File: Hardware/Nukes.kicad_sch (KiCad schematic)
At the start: 25 parts, among them J6 Screw_Terminal_01x08, J7 Conn_01x05_Male, Q2 NCV8415STT1G, Q3 NCV8415STT1G, Q4 NCV8415STT1G, Q5 NCV8415STT1G, U3 LTV-247, U4 PCA9534RGVR, U5 PCA9685BS

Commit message: v3 hardware start
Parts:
- removed Q2, Q3, Q4, Q5: NCV8415STT1G, Package_TO_SOT_SMD:SOT-223, symbol Driver_FET:NCV8402xST
- added Q2, Q3, Q4, Q5: BUK9M11-40EX, Package_TO_SOT_SMD:LFPAK33, symbol Transistor_FET:BUK9M11-40EX
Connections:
- net SERVO4 is gone; now on net SERVO3: J7.5 (Pin_5), U5.14 (LED10)
- net Cont1: now also R18.1, U3.13, U4.4 (P2); no longer R22.1, U3.9, U4.9 (P6)
- net Cont3: now also R22.1, U3.9, U4.9 (P6); no longer R18.1, U3.13, U4.4 (P2)
- net GND: now also Q2.1 (S), Q2.2 (S), Q2.3 (S), Q3.1 (S), Q3.2 (S), Q3.3 (S), Q4.1 (S), Q4.2 (S), Q4.3 (S), Q5.1 (S), Q5.2 (S), Q5.3 (S)
- net Nuke1: now also U4.5 (P3), Q2.4 (G); no longer U4.10 (P7)
- net Nuke1-: now also D8.1 (A), D8.2 (A), J6.3 (Pin_3), U3.3; no longer D10.1 (A), D10.2 (A), J6.7 (Pin_7), U3.7
- net Nuke2: now also Q5.4 (G)
- net Nuke3: now also U4.10 (P7), Q4.4 (G); no longer U4.5 (P3)
- net Nuke3-: now also D10.1 (A), D10.2 (A), J6.7 (Pin_7), U3.7; no longer D8.1 (A), D8.2 (A), J6.3 (Pin_3), U3.3
- net SERVO1: now also J7.3 (Pin_3), U5.12 (LED8); no longer J7.2 (Pin_2), U5.10 (LED7)
- net SERVO2: now also J7.4 (Pin_4), U5.13 (LED9); no longer J7.3 (Pin_3), U5.12 (LED8)
- net SERVO3: no longer J7.4 (Pin_4), U5.13 (LED9)
- net at D10.3 (K): now also Q4.5 (D)
- net at D7.3 (K): now also Q3.5 (D)
- net at D9.3 (K): now also Q5.5 (D)
- net at D8.3 (K): now also Q2.5 (D)
- net Cont4 renamed Cont0
- net Nuke4 renamed Nuke0
- net Nuke0: now also Q3.4 (G)
- net Nuke4- renamed Nuke0-
- new net SERVO0: J7.2 (Pin_2), U5.10 (LED7)

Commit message: more hardware updates
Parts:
- removed R19, R20, R23, R24: 1K, Resistor_SMD:R_0603_1608Metric, symbol Device:R
- added D14, D15, D16, D17: S-102T, iclr-hw:SODFL3516X70N, symbol iclr-hw:S-102T
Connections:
- net GND: now also D14.1 (K), D15.1 (K), D16.1 (K), D17.1 (K)
- net at U3.2: now also D17.2 (A)
- net at U3.4: now also D14.2 (A)
- net at U3.6: now also D16.2 (A)
- net at U3.8: now also D15.2 (A)
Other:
- moved on the sheet: D10, D7, D8, D9, Q2, Q3, Q4, Q5, R17, R18, R21, R22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

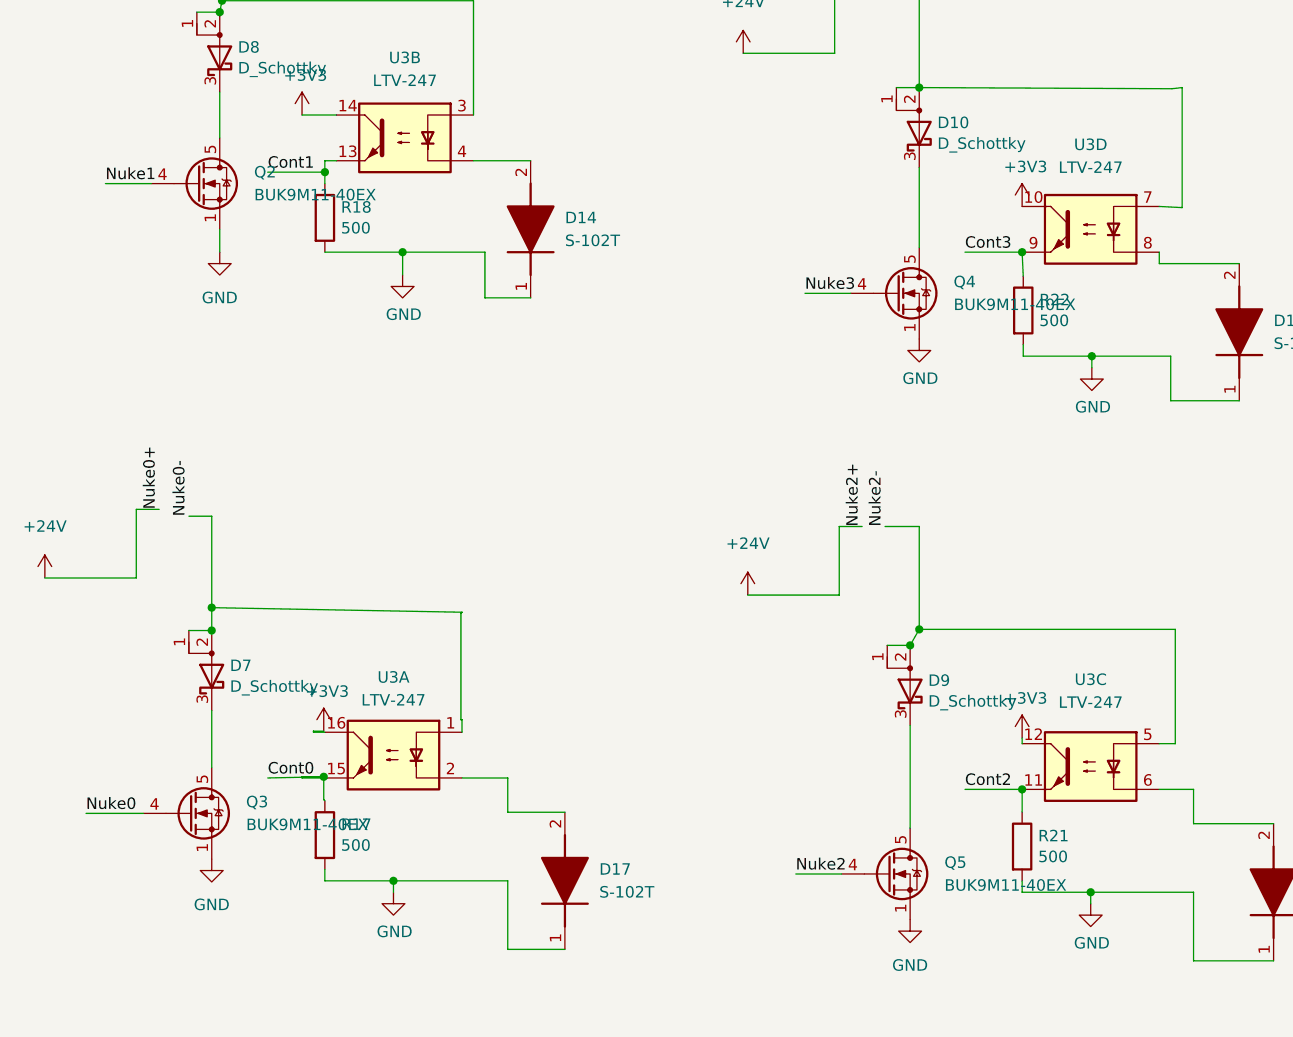
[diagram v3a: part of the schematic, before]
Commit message: added cont and firing leds
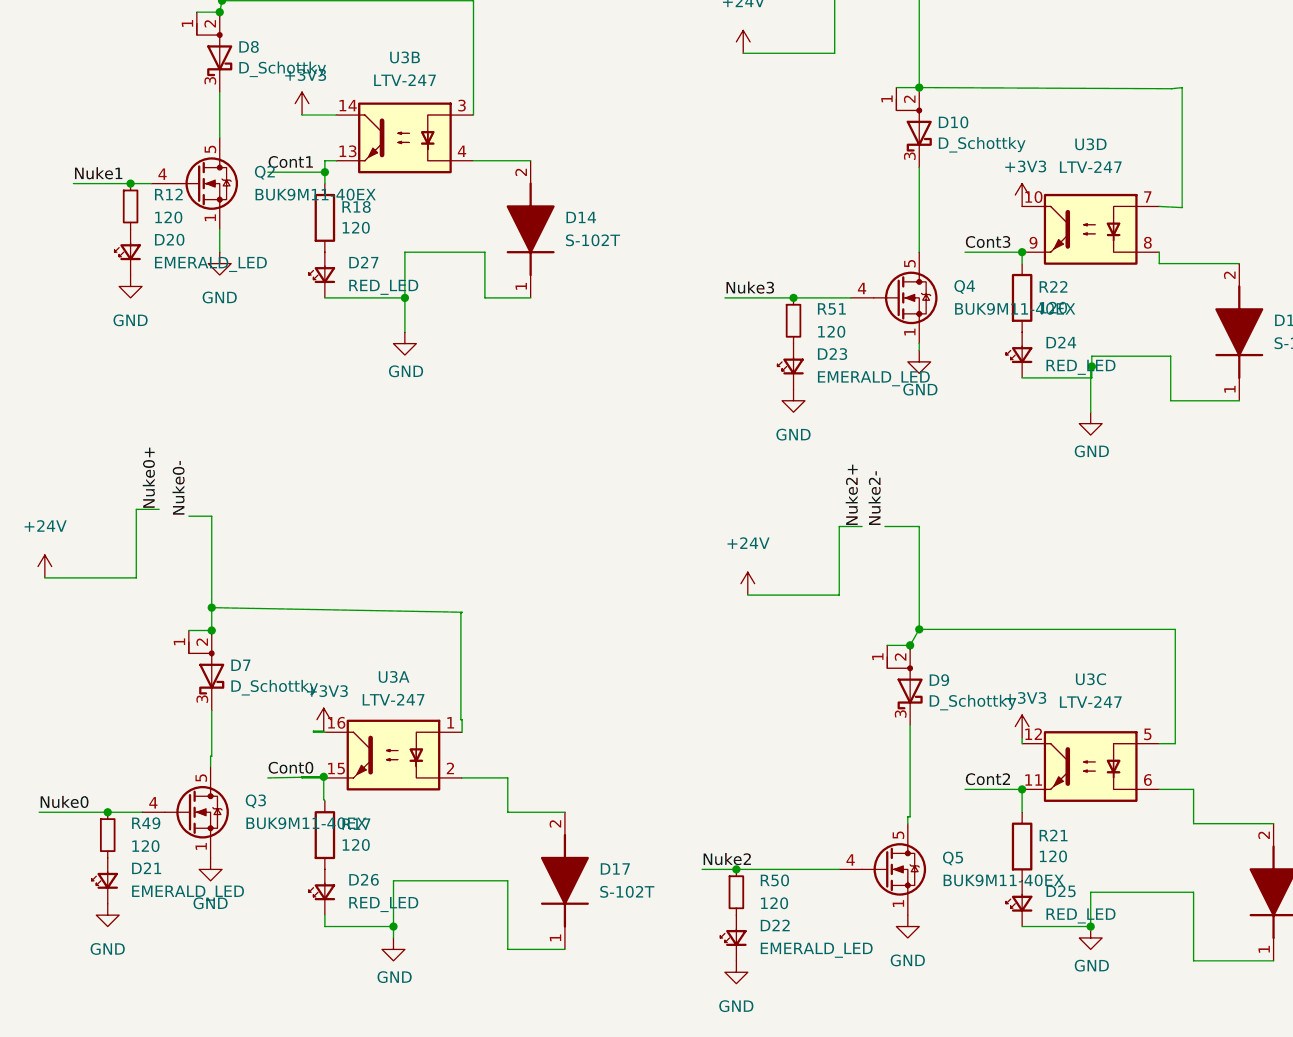
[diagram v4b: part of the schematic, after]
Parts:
- added D20, D21, D22, D23: EMERALD_LED, LED_SMD:LED_0402_1005Metric, symbol Device:LED_Small
- added D24, D25, D26, D27: RED_LED, LED_SMD:LED_0402_1005Metric, symbol Device:LED_Small
- added R12, R49, R50, R51: 120, Resistor_SMD:R_0402_1005Metric, symbol Device:R_Small
- R17, R18, R21, R22: value 500 -> 120
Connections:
- net GND: now also D20.1 (K), D21.1 (K), D22.1 (K), D23.1 (K), D24.1 (K), D25.1 (K), D26.1 (K), D27.1 (K); no longer R17.2, R18.2, R21.2, R22.2
- net Nuke0: now also R49.1
- net Nuke1: now also R12.1
- net Nuke2: now also R50.1
- net Nuke3: now also R51.1
- new net: D27.2 (A), R18.2
- new net: D24.2 (A), R22.2
- new net: D22.2 (A), R50.2
- new net: D21.2 (A), R49.2
- new net: D20.2 (A), R12.2
- new net: D26.2 (A), R17.2
- new net: D23.2 (A), R51.2
- new net: D25.2 (A), R21.2
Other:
- moved on the sheet: Q4, Q5, R22

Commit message: fixes
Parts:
- removed Q2, Q3, Q4, Q5: BUK9M11-40EX, Package_TO_SOT_SMD:LFPAK33, symbol Transistor_FET:BUK9M11-40EX
- added Q2, Q3, Q4, Q6: BSZ025N04LS, iclr-hw:BSZ025N04LS, symbol iclr-hw:BSZ025N04LS
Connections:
- net GND: now also Q2.1 (S), Q2.2 (S), Q2.3 (S), Q2.A1 (S), Q3.1 (S), Q3.2 (S), Q3.3 (S), Q3.A1 (S), Q4.1 (S), Q4.2 (S), Q4.3 (S), Q4.A1 (S), Q6.1 (S), Q6.2 (S), Q6.3 (S), Q6.A1 (S)
- net Nuke0: now also Q3.4 (G)
- net Nuke1: now also Q2.4 (G)
- net Nuke2: now also Q6.4 (G)
- net Nuke3: now also Q4.4 (G)
- net at D8.3 (K): now also Q2.5 (D), Q2.6 (D), Q2.7 (D), Q2.8 (D), Q2.A5 (D)
- net at D9.3 (K): now also Q6.5 (D), Q6.6 (D), Q6.7 (D), Q6.8 (D), Q6.A5 (D)
- net at D10.3 (K): now also Q4.5 (D), Q4.6 (D), Q4.7 (D), Q4.8 (D), Q4.A5 (D)
- net at D7.3 (K): now also Q3.5 (D), Q3.6 (D), Q3.7 (D), Q3.8 (D), Q3.A5 (D)
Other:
- moved on the sheet: D10, D14, D15, D16, D17, D20, D21, D22, D23, D24, D25, D26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

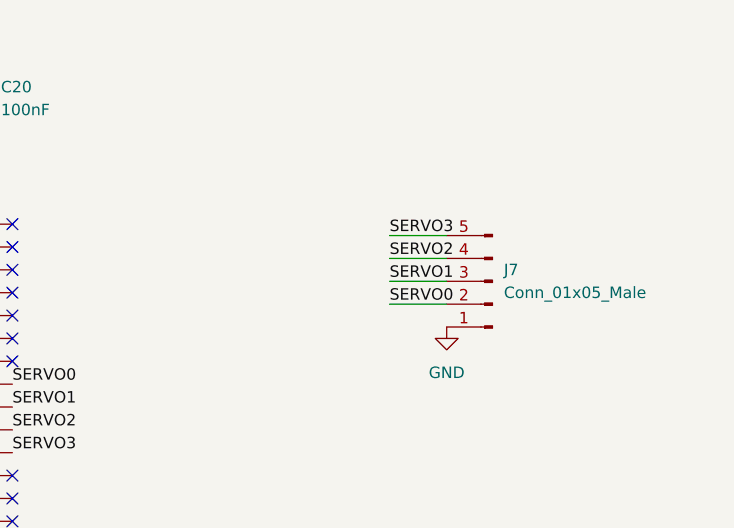
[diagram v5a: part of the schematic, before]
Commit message: updated hardware with current limitng resistors on pwm outputs
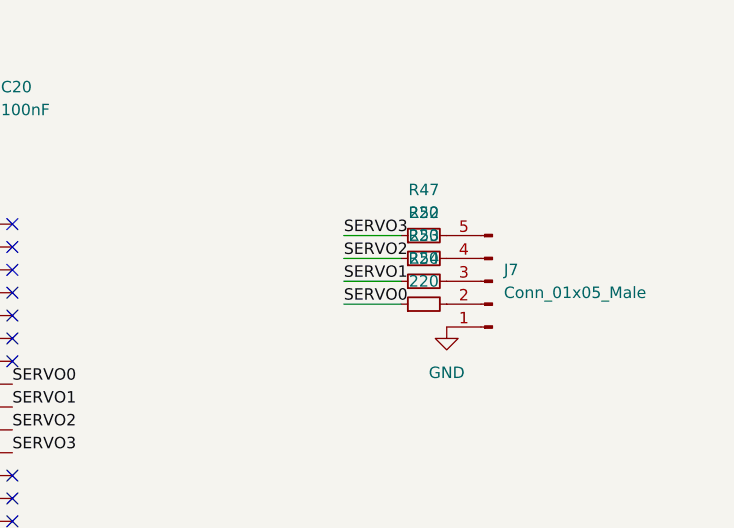
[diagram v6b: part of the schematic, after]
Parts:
- added R47, R52, R53, R54: 220, Resistor_SMD:R_0402_1005Metric, symbol Device:R_Small
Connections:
- net SERVO0: now also R54.1; no longer J7.2 (Pin_2)
- net SERVO1: now also R53.1; no longer J7.3 (Pin_3)
- net SERVO2: now also R52.1; no longer J7.4 (Pin_4)
- net SERVO3: now also R47.1; no longer J7.5 (Pin_5)
- new net: J7.4 (Pin_4), R52.2
- new net: J7.2 (Pin_2), R54.2
- new net: J7.3 (Pin_3), R53.2
- new net: J7.5 (Pin_5), R47.2

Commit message: update
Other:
- note added: "dec 64 : hex 0x40"
- note removed: "dec 128 : hex 0x80"
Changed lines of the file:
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@@
 		)
 	)
-	(text "dec 128 : hex 0x80\n"
+	(text "dec 64 : hex 0x40\n"
 		(exclude_from_sim no)
 		(at 149.86 57.15 0)

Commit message: Adding some 3d models
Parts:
- D14, D15, D16, D17: footprint iclr-hw:SODFL3516X70N -> iclr:SODFL3516X70N
- Q2, Q3, Q4, Q6: footprint iclr-hw:BSZ025N04LS -> iclr:BSZ025N04LS
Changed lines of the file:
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@@
 	(label "Nuke0"
 		(at 34.29 170.18 0)
-		(fields_autoplaced yes)
 		(effects
 			(font
@@
 	(label "Cont2"
 		(at 104.775 48.895 180)
-		(fields_autoplaced yes)
 		(effects
 			(font
@@
 	(label "Nuke1+"
 		(at 43.434 73.66 90)
-		(fields_autoplaced yes)
 		(effects
 			(font
@@
 	(label "Nuke0+"
 		(at 47.625 136.525 90)
-		(fields_autoplaced yes)
 		(effects
 			(font
@@
 	(label "Nuke1"
 		(at 50.8 56.515 0)
-		(fields_autoplaced yes)
 		(effects
 			(font
@@
 	(label "Nuke2"
 		(at 104.775 51.435 180)
-		(fields_autoplaced yes)
 		(effects
 			(font
@@
 	(label "Nuke1-"
 		(at 123.19 57.15 270)
-		(fields_autoplaced yes)
 		(effects
 			(font
@@
 	(label "Nuke1+"
 		(at 125.73 57.15 270)
-		(fields_autoplaced yes)
 		(effects
 			(font
@@
 	(label "_SCL"
 		(at 154.94 36.83 0)
-		(fields_autoplaced yes)
 		(effects
 			(font
@@
 	(label "Nuke3-"
 		(at 228.092 97.155 90)
-		(fields_autoplaced yes)
 		(effects
 			(font
@@
 	(label "Nuke2-"
 		(at 128.27 57.15 270)
-		(fields_autoplaced yes)
 		(effects
 			(font
@@
 	(label "Nuke1-"
 		(at 45.974 73.66 90)
-		(fields_autoplaced yes)
 		(effects
 			(font
@@
 	(label "SERVO2"
 		(at 201.93 59.69 0)
-		(fields_autoplaced yes)
 		(effects
 			(font
@@
 	(label "Cont0"
 		(at 59.69 166.37 0)
-		(fields_autoplaced yes)
 		(effects
 			(font
@@
 	(label "Cont3"
 		(at 237.49 126.873 0)
-		(fields_autoplaced yes)
 		(effects
 			(font
@@
 	(label "Cont3"
 		(at 104.775 53.975 180)
-		(fields_autoplaced yes)
 		(effects
 			(font
@@
 	(label "Nuke3+"
 		(at 225.552 97.155 90)
-		(fields_autoplaced yes)
 		(effects
 			(font
@@
 	(label "SERVO1"
 		(at 201.93 57.15 0)
-		(fields_autoplaced yes)
 		(effects
 			(font
@@
 	(label "Nuke3"
 		(at 210.82 132.08 0)
-		(fields_autoplaced yes)
 		(effects
 			(font
@@
 	(label "Nuke2-"
 		(at 137.16 96.52 90)
-		(fields_autoplaced yes)
 		(effects
 			(font
@@
 	(label "Nuke2+"
 		(at 130.81 57.15 270)
-		(fields_autoplaced yes)
 		(effects
 			(font
@@
 	(label "_SDA"
 		(at 154.94 39.37 0)
-		(fields_autoplaced yes)
 		(effects
 			(font
@@
 	(label "Cont1"
 		(at 50.8 53.975 0)
-		(fields_autoplaced yes)
 		(effects
 			(font
@@
 	(label "Nuke3-"
 		(at 133.35 57.15 270)
-		(fields_autoplaced yes)
 		(effects
 			(font
@@
 	(label "SERVO2"
 		(at 238.76 40.64 0)
-		(fields_autoplaced yes)
 		(effects
 			(font
@@
 	(label "Nuke0-"
 		(at 118.11 57.15 270)
-		(fields_autoplaced yes)
 		(effects
 			(font
@@
 	(label "Nuke0-"
 		(at 50.927 137.287 90)
-		(fields_autoplaced yes)
 		(effects
 			(font
@@
 	(label "Nuke1"
 		(at 27.94 105.41 0)
-		(fields_autoplaced yes)
 		(effects
 			(font
@@
 	(label "SERVO3"
 		(at 238.76 38.1 0)
-		(fields_autoplaced yes)
 		(effects
 			(font
@@
 	(label "Cont1"
 		(at 54.864 104.14 0)
-		(fields_autoplaced yes)
 		(effects
 			(font
@@
 	(label "Cont0"
 		(at 50.8 48.895 0)
-		(fields_autoplaced yes)
 		(effects
 			(font
@@
 	(label "SERVO1"
 		(at 238.76 43.18 0)
-		(fields_autoplaced yes)
 		(effects
 			(font
@@
 	(label "_SCL"
 		(at 50.8 43.815 0)
-		(fields_autoplaced yes)
 		(effects
 			(font
@@
 	(label "_SCL"
 		(at 36.195 25.4 0)
-		(fields_autoplaced yes)
 		(effects
 			(font
@@
 	(label "SERVO3"
 		(at 201.93 62.23 0)
-		(fields_autoplaced yes)
 		(effects
 			(font
@@
 	(label "Nuke3+"
 		(at 135.89 57.15 270)
-		(fields_autoplaced yes)
 		(effects
 			(font
@@
 	(label "Nuke3"
 		(at 104.775 56.515 180)
-		(fields_autoplaced yes)
 		(effects
 			(font
@@
 	(label "Nuke0"
 		(at 50.8 51.435 0)
-		(fields_autoplaced yes)
 		(effects
 			(font
@@
 	(label "Nuke2"
 		(at 116.84 134.62 0)
-		(fields_autoplaced yes)
 		(effects
 			(font
@@
 	(label "_SDA"
 		(at 35.56 29.21 0)
-		(fields_autoplaced yes)
 		(effects
 			(font
@@
 	(label "Cont2"
 		(at 146.05 125.73 0)
-		(fields_autoplaced yes)
 		(effects
 			(font
@@
 	(label "SERVO0"
 		(at 201.93 54.61 0)
-		(fields_autoplaced yes)
 		(effects
 			(font
@@
 	(label "Nuke0+"
 		(at 120.65 57.15 270)
-		(fields_autoplaced yes)
 		(effects
 			(font
@@
 	(label "_SDA"
 		(at 50.8 61.595 0)
-		(fields_autoplaced yes)
 		(effects
 			(font
@@
 	(label "SERVO0"
 		(at 238.76 45.72 0)
-		(fields_autoplaced yes)
 		(effects
 			(font
@@
 	(label "Nuke2+"
 		(at 134.62 96.52 90)
-		(fields_autoplaced yes)
 		(effects
 			(font
@@
 		(shape input)
 		(at 28.575 29.21 180)
-		(fields_autoplaced yes)
 		(effects
 			(font
@@
 		(shape input)
 		(at 28.575 25.4 180)
-		(fields_autoplaced yes)
 		(effects
 			(font
@@
 			)
 		)
-		(property "Footprint" "iclr-hw:BSZ025N04LS"
+		(property "Footprint" "iclr:BSZ025N04LS"
 			(at 160.02 229.54 0)
 			(effects
@@
 			)
 		)
-		(property "Footprint" "iclr-hw:BSZ025N04LS"
+		(property "Footprint" "iclr:BSZ025N04LS"
 			(at 73.66 265.1 0)
 			(effects
@@
 			)
 		)
-		(property "Footprint" "iclr-hw:BSZ025N04LS"
+		(property "Footprint" "iclr:BSZ025N04LS"
 			(at 252.73 227 0)
 			(effects
@@
 			)
 		)
-		(property "Footprint" "iclr-hw:SODFL3516X70N"
+		(property "Footprint" "iclr:SODFL3516X70N"
 			(at 277.8 133.35 0)
 			(effects
@@
 			)
 		)
-		(property "Footprint" "iclr-hw:SODFL3516X70N"
+		(property "Footprint" "iclr:SODFL3516X70N"
 			(at 365.43 131.953 0)
 			(effects
@@
 			)
 		)
-		(property "Footprint" "iclr-hw:SODFL3516X70N"
+		(property "Footprint" "iclr:SODFL3516X70N"
 			(at 181.534 106.68 0)
 			(effects
@@
 			)
 		)
-		(property "Footprint" "iclr-hw:SODFL3516X70N"
+		(property "Footprint" "iclr:SODFL3516X70N"
 			(at 190.17 173.99 0)
 			(effects
@@
 			)
 		)
-		(property "Footprint" "iclr-hw:BSZ025N04LS"
+		(property "Footprint" "iclr:BSZ025N04LS"
 			(at 69.85 200.33 0)
 			(effects
